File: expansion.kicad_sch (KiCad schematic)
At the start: 13 parts, among them J2 Arduino Mega, J3 Expansion, J4 Logic Probe, J5 Barrel Jack, SW2 Power

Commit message: intermediate commit
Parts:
- removed D10: A10-A15/CLK/IRQ, digikey-footprints:LED_Bar_Graph_LTA-1000, symbol dk_LEDs-Circuit-Board-Indicators-Arrays-Light-Bars-Bar-Graphs:LTA-1000Y
- removed D8: DATA, digikey-footprints:LED_Bar_Graph_LTA-1000, symbol dk_LEDs-Circuit-Board-Indicators-Arrays-Light-Bars-Bar-Graphs:LTA-1000Y
- removed D9: A0-A9, digikey-footprints:LED_Bar_Graph_LTA-1000, symbol dk_LEDs-Circuit-Board-Indicators-Arrays-Light-Bars-Bar-Graphs:LTA-1000Y
- removed J2: Arduino Mega, Connector_PinSocket_2.54mm:PinSocket_2x16_P2.54mm_Vertical, symbol Connector_Generic:Conn_02x16_Odd_Even
- removed J3: Expansion, Connector_PinSocket_2.54mm:PinSocket_2x16_P2.54mm_Vertical, symbol Connector_Generic:Conn_02x16_Odd_Even
- removed RN1: D0-7, Resistor_THT:R_Array_SIP11, symbol Device:R_Network10
- removed RN2: A0-A9, Resistor_THT:R_Array_SIP11, symbol Device:R_Network10
- removed RN3: A10-A15/CLK/IRQ, Resistor_THT:R_Array_SIP11, symbol Device:R_Network10
- added Buttom1: Middle, Button_Switch_THT:SW_PUSH_6mm_H5mm, symbol Switch:SW_Push
- added C15: .1uf, Capacitor_THT:C_Disc_D4.3mm_W1.9mm_P5.00mm, symbol Device:C
- added D6: Power, LED_THT:LED_D5.0mm, symbol Device:LED
- added D7: SB140, Diode_THT:D_DO-41_SOD81_P10.16mm_Horizontal, symbol Diode:SB140
- added J2: Conn_01x02, Connector_PinSocket_1.27mm:PinSocket_1x02_P1.27mm_Vertical, symbol Connector_Generic:Conn_01x02
- added J5, J6: Conn_02x20_Counter_Clockwise, Connector_PinSocket_1.27mm:PinSocket_2x20_P1.27mm_Vertical, symbol Connector_Generic:Conn_02x20_Counter_Clockwise
- added Left1: Right, Button_Switch_THT:SW_PUSH_6mm_H5mm, symbol Switch:SW_Push
- added Middle1: Top, Button_Switch_THT:SW_PUSH_6mm_H5mm, symbol Switch:SW_Push
- added R15, R16, R17, R18, R19: 1K, Resistor_THT:R_Axial_DIN0207_L6.3mm_D2.5mm_P7.62mm_Horizontal, symbol Device:R
- added R17: 220, Resistor_THT:R_Axial_DIN0207_L6.3mm_D2.5mm_P7.62mm_Horizontal, symbol Device:R
- added Right1: Bottom, Button_Switch_THT:SW_PUSH_6mm_H5mm, symbol Switch:SW_Push
- added Top1: Left, Button_Switch_THT:SW_PUSH_6mm_H5mm, symbol Switch:SW_Push
- added U11: W65C22NxP, Package_DIP:DIP-40_W15.24mm, symbol PCM_65xx-library:W65C22NxP
- renumbered J5 to J3, R14 to R18
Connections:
- net +5V: now also SW2.1 (A), C15.1, J5.20 (Pin_20), J6.20 (Pin_20), R15.2, R16.2, R17.1, R17.2, R18.2, R19.2, U11.20 (VCC); no longer SW2.3 (C)
- net A0: now also J5.1 (Pin_1), J6.1 (Pin_1), U11.38 (RS0)
- net A1: now also J5.2 (Pin_2), J6.2 (Pin_2), U11.37 (RS1)
- net A10: now also J5.11 (Pin_11), J6.11 (Pin_11)
- net A11: now also J5.12 (Pin_12), J6.12 (Pin_12)
- net A12: now also J5.13 (Pin_13), J6.13 (Pin_13)
- net A13: now also J5.14 (Pin_14), J6.14 (Pin_14), U11.24 (CS1)
- net A14: now also J5.15 (Pin_15), J6.15 (Pin_15)
- net A15: now also J5.16 (Pin_16), J6.16 (Pin_16)
- net A2: now also J5.3 (Pin_3), J6.3 (Pin_3), U11.36 (RS2)
- net A3: now also J5.4 (Pin_4), J6.4 (Pin_4), U11.35 (RS3)
- net A4: now also J5.5 (Pin_5), J6.5 (Pin_5)
- net A5: now also J5.6 (Pin_6), J6.6 (Pin_6)
- net A6: now also J5.7 (Pin_7), J6.7 (Pin_7)
- net A7: now also J5.8 (Pin_8), J6.8 (Pin_8)
- net A8: now also J5.9 (Pin_9), J6.9 (Pin_9)
- net A9: now also J5.10 (Pin_10), J6.10 (Pin_10)
- net BE: now also J5.25 (Pin_25), J6.25 (Pin_25)
- net CLK: now also J5.31 (Pin_31), J6.31 (Pin_31), U11.25 (ϕ2)
- net D0: now also J5.40 (Pin_40), J6.40 (Pin_40), U11.33 (D0)
- net D1: now also J5.39 (Pin_39), J6.39 (Pin_39), U11.32 (D1)
- net D2: now also J5.38 (Pin_38), J6.38 (Pin_38), U11.31 (D2)
- net D3: now also J5.37 (Pin_37), J6.37 (Pin_37), U11.30 (D3)
- net D4: now also J5.36 (Pin_36), J6.36 (Pin_36), U11.29 (D4)
- net D5: now also J5.35 (Pin_35), J6.35 (Pin_35), U11.28 (D5)
- net D6: now also J5.34 (Pin_34), J6.34 (Pin_34), U11.27 (D6)
- net D7: now also J5.33 (Pin_33), J6.33 (Pin_33), U11.26 (D7)
- net Earth: now also J3.2, Buttom1.1, C15.2, D6.1 (K), J2.2 (Pin_2), J5.21 (Pin_21), J6.21 (Pin_21), Left1.1, Middle1.1, Right1.1, Top1.1, U11.1 (VSS); no longer J3.1
- net HLT: now also J5.27 (Pin_27), J6.27 (Pin_27)
- net IRQ: now also D7.2 (A), J5.28 (Pin_28), J6.28 (Pin_28)
- net Reset: now also J5.29 (Pin_29), J6.29 (Pin_29), U11.34 (~{RES})
- net R/W: now also J5.30 (Pin_30), J6.30 (Pin_30), U11.22 (R/~{W})
- net Sync: now also J5.26 (Pin_26), J6.26 (Pin_26)
- net at SW2.2 (B): now also J3.1, J2.1 (Pin_1); no longer J3.2
- new net: Left1.2, R18.1, U11.5 (PA3)
- new net: Middle1.2, R15.1, U11.2 (PA0)
- new net: D7.1 (K), U11.21 (~{IRQ})
- new net: R16.1, Top1.2, U11.3 (PA1)
- new net: Buttom1.2, R17.1, U11.4 (PA2)
- new net: R19.1, Right1.2, U11.6 (PA4)
- new net: D6.2 (A), R17.2
- new net CS2Via2: U11.23 (~{CS2})
- no-connect marks 0 -> 14
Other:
- moved on the sheet: J3, SW2

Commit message: interm commit
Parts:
- added D10, D9: 1N4001, Diode_THT:D_DO-41_SOD81_P10.16mm_Horizontal, symbol Diode:1N4001
- added J12, J13: Conn_01x10, Connector_PinSocket_1.27mm:PinSocket_1x10_P1.27mm_Vertical, symbol Connector_Generic:Conn_01x10
- renumbered Right1 to Bottom1, C15 to C19, Top1 to Left1, Buttom1 to Middle1, R15 to R19, R16 to R20, R17 to R21, R18 to R22, R19 to R23, Left1 to Right1, Middle1 to Top1, U11 to U14
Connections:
- net +5V: now also J12.1 (Pin_1), J13.1 (Pin_1)
- net Earth: now also D10.2 (A), J12.10 (Pin_10), J13.10 (Pin_10); no longer J2.2 (Pin_2), J3.2
- net at R22.1, Right1.2, U14.5 (PA3): now also J13.5 (Pin_5)
- net at U14.10 (PB0): now also J12.2 (Pin_2)
- net at U14.11 (PB1): now also J12.3 (Pin_3)
- net at U14.12 (PB2): now also J12.4 (Pin_4)
- net at U14.13 (PB3): now also J12.5 (Pin_5)
- net at U14.14 (PB4): now also J12.6 (Pin_6)
- net at U14.15 (PB5): now also J12.7 (Pin_7)
- net at U14.16 (PB6): now also J12.8 (Pin_8)
- net at U14.17 (PB7): now also J12.9 (Pin_9)
- net at R19.1, Top1.2, U14.2 (PA0): now also J13.2 (Pin_2)
- net at Left1.2, R20.1, U14.3 (PA1): now also J13.3 (Pin_3)
- net at Middle1.2, R21.1, U14.4 (PA2): now also J13.4 (Pin_4)
- net at Bottom1.2, R23.1, U14.6 (PA4): now also J13.6 (Pin_6)
- net at U14.7 (PA5): now also J13.7 (Pin_7)
- net at U14.8 (PA6): now also J13.8 (Pin_8)
- net at U14.9 (PA7): now also J13.9 (Pin_9)
- net at J2.1 (Pin_1), J3.1: now also D9.2 (A); no longer SW2.2 (B)
- new net: D10.1 (K), J2.2 (Pin_2), J3.2
- new net: D9.1 (K), SW2.2 (B)
- no-connect marks 14 -> 18
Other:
- moved on the sheet: J2

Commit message: An other interm relase
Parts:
- J12, J13: footprint Connector_PinSocket_1.27mm:PinSocket_1x10_P1.27mm_Vertical -> Connector_PinSocket_2.54mm:PinSocket_1x10_P2.54mm_Vertical
- J5, J6: footprint Connector_PinSocket_1.27mm:PinSocket_2x20_P1.27mm_Vertical -> Connector_PinSocket_2.54mm:PinSocket_2x20_P2.54mm_Vertical

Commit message: Fix Oops...
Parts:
- removed D10: 1N4001, Diode_THT:D_DO-41_SOD81_P10.16mm_Horizontal, symbol Diode:1N4001
- C19: value .1uf -> 0.1uf
- J2: footprint Connector_PinSocket_1.27mm:PinSocket_1x02_P1.27mm_Vertical -> Connector_PinSocket_2.54mm:PinSocket_1x02_P2.54mm_Vertical
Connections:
- net Earth: now also J2.2 (Pin_2), J3.2
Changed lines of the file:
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@@
 	)
 	(junction
-		(at 153.67 26.035)
-		(diameter 0)
-		(color 0 0 0 0)
-	)
-	(junction
 		(at 112.395 81.915)
 		(diameter 0)
@@
 	)
 	(junction
+		(at 153.67 25.908)
+		(diameter 0)
+		(color 0 0 0 0)
+	)
+	(junction
 		(at 116.205 33.655)
 		(diameter 0)
@@
 	(wire
 		(pts
-			(xy 153.67 24.13) (xy 153.67 26.035)
+			(xy 153.67 24.13) (xy 153.67 25.908)
 		)
 		(stroke
@@
 	(wire
 		(pts
-			(xy 137.16 27.305) (xy 137.16 26.035)
-		)
-		(stroke
-			(width 0)
-			(type default)
-		)
-	)
-	(wire
-		(pts
 			(xy 87.63 75.565) (xy 87.63 82.55)
 		)
@@
 	(wire
 		(pts
-			(xy 137.16 26.035) (xy 139.7 26.035)
-		)
-		(stroke
-			(width 0)
-			(type default)
-		)
-	)
-	(wire
-		(pts
 			(xy 92.71 70.485) (xy 92.71 82.55)
 		)
@@
 	(wire
 		(pts
-			(xy 147.32 26.035) (xy 153.67 26.035)
+			(xy 111.125 65.405) (xy 111.125 69.215)
 		)
 		(stroke
@@
 	(wire
 		(pts
-			(xy 111.125 65.405) (xy 111.125 69.215)
+			(xy 109.855 67.945) (xy 95.25 67.945)
 		)
 		(stroke
@@
 	(wire
 		(pts
-			(xy 109.855 67.945) (xy 95.25 67.945)
+			(xy 97.79 65.405) (xy 97.79 82.55)
 		)
 		(stroke
@@
 	(wire
 		(pts
-			(xy 97.79 65.405) (xy 97.79 82.55)
+			(xy 199.39 72.39) (xy 205.74 72.39)
 		)
 		(stroke
@@
 	(wire
 		(pts
-			(xy 199.39 72.39) (xy 205.74 72.39)
+			(xy 153.67 25.908) (xy 153.67 26.035)
 		)
 		(stroke
@@
 			)
 		)
-		(property "Value" ".1uf"
+		(property "Value" "0.1uf"
 			(at 122.555 160.02 0)
 			(effects
@@
 	(symbol
 		(lib_id "power:Earth")
-		(at 137.16 27.305 0)
+		(at 153.67 25.908 0)
 		(unit 1)
 		(exclude_from_sim no)
@@
 		(fields_autoplaced yes)
 		(property "Reference" "#PWR034"
-			(at 137.16 33.655 0)
+			(at 153.67 32.258 0)
 			(effects
 				(font
@@
 		)
 		(property "Value" "Earth"
-			(at 137.16 31.115 0)
+			(at 153.67 29.718 0)
 			(effects
 				(font
@@
 		)
 		(property "Footprint" ""
-			(at 137.16 27.305 0)
+			(at 153.67 25.908 0)
 			(effects
 				(font
@@
 		)
 		(property "Datasheet" "~"
-			(at 137.16 27.305 0)
+			(at 153.67 25.908 0)
 			(effects
 				(font
@@
 		)
 		(property "Description" ""
-			(at 137.16 27.305 0)
+			(at 153.67 25.908 0)
 			(effects
 				(font
@@
 			)
 		)
-		(property "Footprint" "Connector_PinSocket_1.27mm:PinSocket_1x02_P1.27mm_Vertical"
+		(property "Footprint" "Connector_PinSocket_2.54mm:PinSocket_1x02_P2.54mm_Vertical"
 			(at 151.13 19.05 0)
 			(effects
@@
 					(unit 1)
 				)
-			)
-		)
-	)
-	(symbol
-		(lib_id "Diode:1N4001")
-		(at 143.51 26.035 180)
-		(unit 1)
-		(exclude_from_sim no)
-		(in_bom yes)
-		(on_board yes)
-		(dnp no)
-		(property "Reference" "D10"
-			(at 146.685 24.765 0)
-			(effects
-				(font
-					(size 1.27 1.27)
-				)
-			)
-		)
-		(property "Value" "1N4001"
-			(at 144.145 22.86 0)
-			(effects
-				(font
-					(size 1.27 1.27)
-				)
-			)
-		)
-		(property "Footprint" "Diode_THT:D_DO-41_SOD81_P10.16mm_Horizontal"
-			(at 143.51 26.035 0)
-			(effects
-				(font
-					(size 1.27 1.27)
-				)
-				(hide yes)
-			)
-		)
-		(property "Datasheet" "http://www.vishay.com/docs/88503/1n4001.pdf"
-			(at 143.51 26.035 0)
-			(effects
-				(font
-					(size 1.27 1.27)
-				)
-				(hide yes)
-			)
-		)
-		(property "Description" "50V 1A General Purpose Rectifier Diode, DO-41"
-			(at 143.51 26.035 0)
-			(effects
-				(font
-					(size 1.27 1.27)
-				)
-				(hide yes)
-			)
-		)
-		(property "Sim.Device" "D"
-			(at 143.51 26.035 0)
-			(effects
-				(font
-					(size 1.27 1.27)
-				)
-				(hide yes)
-			)
-		)
-		(property "Sim.Pins" "1=K 2=A"
-			(at 143.51 26.035 0)
-			(effects
-				(font
-					(size 1.27 1.27)
-				)
-				(hide yes)
-			)
-		)
-		(pin "2"
-		)
-		(pin "1"
-		)
-		(instances
-			(project "BenEater-6502"
-				(path "/64020bd5-bae0-49a1-9410-23726bcfaf48/16aa598a-cc79-4ffe-8299-2b52f0e64f5a"
-					(reference "D10")
-					(unit 1)
-				)

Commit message: Closer yet
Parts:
- removed D7: SB140, Diode_THT:D_DO-41_SOD81_P10.16mm_Horizontal, symbol Diode:SB140
- J5, J6: symbol Connector_Generic:Conn_02x20_Counter_Clockwise -> Connector_Generic:Conn_02x20_Odd_Even
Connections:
- net +5V: now also J5.39 (Pin_39), J6.39 (Pin_39); no longer J5.20 (Pin_20), J6.20 (Pin_20)
- net A1: now also J5.3 (Pin_3), J6.3 (Pin_3); no longer J5.2 (Pin_2), J6.2 (Pin_2)
- net A10: now also J5.21 (Pin_21), J6.21 (Pin_21); no longer J5.11 (Pin_11), J6.11 (Pin_11)
- net A11: now also J5.23 (Pin_23), J6.23 (Pin_23); no longer J5.12 (Pin_12), J6.12 (Pin_12)
- net A12: now also J5.25 (Pin_25), J6.25 (Pin_25); no longer J5.13 (Pin_13), J6.13 (Pin_13)
- net A13: now also J5.27 (Pin_27), J6.27 (Pin_27); no longer J5.14 (Pin_14), J6.14 (Pin_14)
- net A14: now also J5.29 (Pin_29), J6.29 (Pin_29); no longer J5.15 (Pin_15), J6.15 (Pin_15)
- net A15: now also J5.31 (Pin_31), J6.31 (Pin_31); no longer J5.16 (Pin_16), J6.16 (Pin_16)
- net A2: now also J5.5 (Pin_5), J6.5 (Pin_5); no longer J5.3 (Pin_3), J6.3 (Pin_3)
- net A3: now also J5.7 (Pin_7), J6.7 (Pin_7); no longer J5.4 (Pin_4), J6.4 (Pin_4), U14.35 (RS3)
- net A4: now also J5.9 (Pin_9), J6.9 (Pin_9), U14.35 (RS3); no longer J5.5 (Pin_5), J6.5 (Pin_5)
- net A5: now also J5.11 (Pin_11), J6.11 (Pin_11); no longer J5.6 (Pin_6), J6.6 (Pin_6)
- net A6: now also J5.13 (Pin_13), J6.13 (Pin_13); no longer J5.7 (Pin_7), J6.7 (Pin_7)
- net A7: now also J5.15 (Pin_15), J6.15 (Pin_15); no longer J5.8 (Pin_8), J6.8 (Pin_8)
- net A8: now also J5.17 (Pin_17), J6.17 (Pin_17); no longer J5.9 (Pin_9), J6.9 (Pin_9)
- net A9: now also J5.19 (Pin_19), J6.19 (Pin_19); no longer J5.10 (Pin_10), J6.10 (Pin_10)
- net BE: now also J5.32 (Pin_32), J6.32 (Pin_32); no longer J5.25 (Pin_25), J6.25 (Pin_25)
- net CLK: now also J5.20 (Pin_20), J6.20 (Pin_20); no longer J5.31 (Pin_31), J6.31 (Pin_31)
- net D0: now also J5.2 (Pin_2), J6.2 (Pin_2); no longer J5.40 (Pin_40), J6.40 (Pin_40)
- net D1: now also J5.4 (Pin_4), J6.4 (Pin_4); no longer J5.39 (Pin_39), J6.39 (Pin_39)
- net D2: now also J5.6 (Pin_6), J6.6 (Pin_6); no longer J5.38 (Pin_38), J6.38 (Pin_38)
- net D3: now also J5.8 (Pin_8), J6.8 (Pin_8); no longer J5.37 (Pin_37), J6.37 (Pin_37)
- net D4: now also J5.10 (Pin_10), J6.10 (Pin_10); no longer J5.36 (Pin_36), J6.36 (Pin_36)
- net D5: now also J5.12 (Pin_12), J6.12 (Pin_12); no longer J5.35 (Pin_35), J6.35 (Pin_35)
- net D6: now also J5.14 (Pin_14), J6.14 (Pin_14); no longer J5.34 (Pin_34), J6.34 (Pin_34)
- net D7: now also J5.16 (Pin_16), J6.16 (Pin_16); no longer J5.33 (Pin_33), J6.33 (Pin_33)
- net Earth: now also J5.40 (Pin_40), J6.40 (Pin_40); no longer J5.21 (Pin_21), J6.21 (Pin_21)
- net HLT: now also J5.28 (Pin_28), J6.28 (Pin_28); no longer J5.27 (Pin_27), J6.27 (Pin_27)
- net IRQ: now also J5.26 (Pin_26), J6.26 (Pin_26), U14.21 (~{IRQ}); no longer J5.28 (Pin_28), J6.28 (Pin_28)
- net Reset: now also J5.24 (Pin_24), J6.24 (Pin_24); no longer J5.29 (Pin_29), J6.29 (Pin_29)
- net R/W: now also J5.22 (Pin_22), J6.22 (Pin_22); no longer J5.30 (Pin_30), J6.30 (Pin_30)
- net Sync: now also J5.30 (Pin_30), J6.30 (Pin_30); no longer J5.26 (Pin_26), J6.26 (Pin_26)
- net CS2Via2 renamed CS2
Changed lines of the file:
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@@
 	(wire
 		(pts
-			(xy 20.32 70.485) (xy 26.035 70.485)
-		)
-		(stroke
-			(width 0)
-			(type default)
-		)
-	)
-	(wire
-		(pts
 			(xy 199.39 62.23) (xy 205.74 62.23)
 		)
@@
 		)
 	)
+	(hierarchical_label "CS2"
+		(shape bidirectional)
+		(at 34.925 78.105 180)
+		(fields_autoplaced yes)
+		(effects
+			(font
+				(size 1.27 1.27)
+			)
+			(justify right)
+		)
+	)
 	(hierarchical_label "A8"
 		(shape bidirectional)
@@
 		)
 	)
+	(hierarchical_label "A4"
+		(shape bidirectional)
+		(at 34.925 90.805 180)
+		(fields_autoplaced yes)
+		(effects
+			(font
+				(size 1.27 1.27)
+			)
+			(justify right)
+		)
+	)
 	(hierarchical_label "A1"
 		(shape bidirectional)
@@
 		)
 	)
-	(hierarchical_label "CS2Via2"
-		(shape bidirectional)
-		(at 34.925 78.105 180)
-		(fields_autoplaced yes)
-		(effects
-			(font
-				(size 1.27 1.27)
-			)
-			(justify right)
-		)
-	)
 	(hierarchical_label "A11"
 		(shape bidirectional)
@@
 		)
 	)
-	(hierarchical_label "A3"
-		(shape bidirectional)
-		(at 34.925 90.805 180)
-		(fields_autoplaced yes)
-		(effects
-			(font
-				(size 1.27 1.27)
-			)
-			(justify right)
-		)
-	)
 	(hierarchical_label "A7"
 		(shape bidirectional)
@@
 	(hierarchical_label "IRQ"
 		(shape bidirectional)
-		(at 20.32 70.485 180)
+		(at 33.655 70.485 180)
 		(fields_autoplaced yes)
 		(effects
@@
 	)
 	(symbol
-		(lib_id "Connector_Generic:Conn_02x20_Counter_Clockwise")
+		(lib_id "Connector_Generic:Conn_02x20_Odd_Even")
 		(at 210.82 77.47 0)
 		(unit 1)
@@
 			)
 		)
-		(property "Description" ""
+		(property "Description" "Generic connector, double row, 02x20, odd/even pin numbering scheme (row 1 odd numbers, row 2 even numbers), script generated (kicad-library-utils/schlib/autogen/connector/)"
 			(at 210.82 77.47 0)
 			(effects
@@
 	)
 	(symbol
-		(lib_id "Connector_Generic:Conn_02x20_Counter_Clockwise")
+		(lib_id "Connector_Generic:Conn_02x20_Odd_Even")
 		(at 255.27 77.47 0)
 		(unit 1)
@@
 			)
 		)
-		(property "Description" ""
+		(property "Description" "Generic connector, double row, 02x20, odd/even pin numbering scheme (row 1 odd numbers, row 2 even numbers), script generated (kicad-library-utils/schlib/autogen/connector/)"
 			(at 255.27 77.47 0)
 			(effects
@@
 					(unit 1)
 				)
-			)
-		)
-	)
-	(symbol
-		(lib_id "Diode:SB140")
-		(at 29.845 70.485 180)
-		(unit 1)
-		(exclude_from_sim no)
-		(in_bom yes)
-		(on_board yes)
-		(dnp no)
-		(property "Reference" "D7"
-			(at 26.67 69.215 0)
-			(effects
-				(font
-					(size 1.27 1.27)
-				)
-			)
-		)
-		(property "Value" "SB140"
-			(at 30.1625 66.675 0)
-			(effects
-				(font
-					(size 1.27 1.27)
-				)
-				(hide yes)
-			)
-		)
-		(property "Footprint" "Diode_THT:D_DO-41_SOD81_P10.16mm_Horizontal"
-			(at 29.845 66.04 0)
-			(effects
-				(font
-					(size 1.27 1.27)
-				)
-				(hide yes)
-			)
-		)
-		(property "Datasheet" "http://www.diodes.com/_files/datasheets/ds23022.pdf"
-			(at 29.845 70.485 0)
-			(effects
-				(font
-					(size 1.27 1.27)
-				)
-				(hide yes)
-			)
-		)
-		(property "Description" ""
-			(at 29.845 70.485 0)
-			(effects
-				(font
-					(size 1.27 1.27)
-				)
-				(hide yes)
-			)
-		)
-		(pin "1"
-		)
-		(pin "2"
-		)
-		(instances
-			(project "BenEater-6502"
-				(path "/64020bd5-bae0-49a1-9410-23726bcfaf48/16aa598a-cc79-4ffe-8299-2b52f0e64f5a"
-					(reference "D7")
-					(unit 1)
-				)

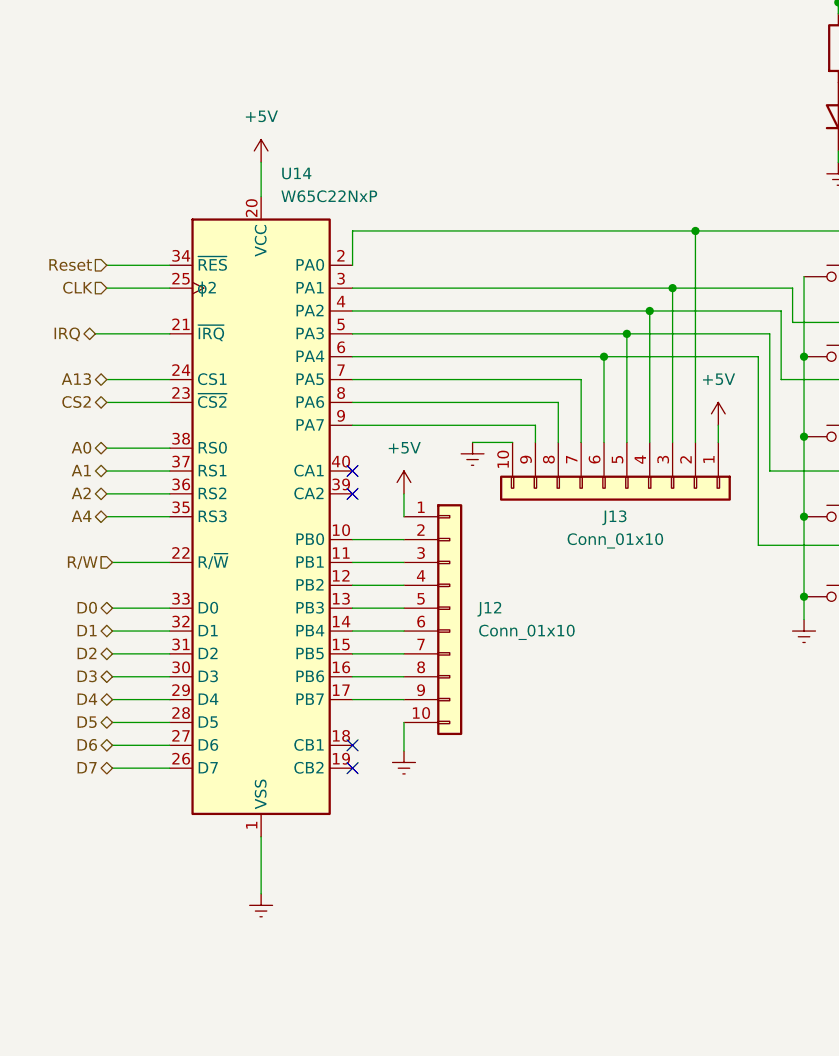
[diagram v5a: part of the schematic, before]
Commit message: Fixed the addressing Still not fixed
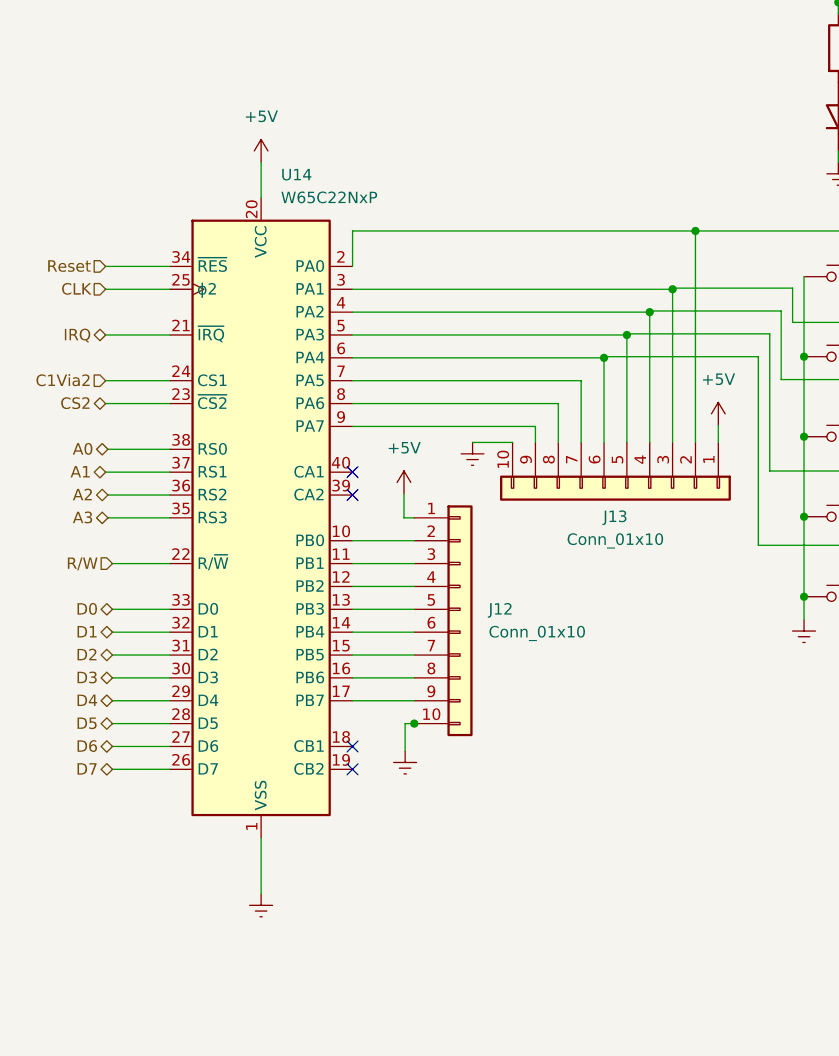
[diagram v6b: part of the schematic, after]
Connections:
- net A13: no longer U14.24 (CS1)
- net A3: now also U14.35 (RS3)
- net A4: no longer U14.35 (RS3)
- new net C1Via2: U14.24 (CS1)
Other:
- moved on the sheet: J12
